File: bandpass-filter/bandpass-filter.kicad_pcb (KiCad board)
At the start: 2 copper layers, 56 x 19 mm, 12 parts, among them J1 Amphenol 10118194-0001LF, J2 Conn_Coaxial, J3 Conn_Coaxial, U1 SKY65015-70LF

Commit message: remove todos
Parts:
- added H1: MountingHole, MountingHole:MountingHole_4.3mm_M4, F.Cu at (98.2, 40.6)
- added H2: MountingHole, MountingHole:MountingHole_4.3mm_M4, F.Cu at (145.2, 40.6)
- added H3: MountingHole, MountingHole:MountingHole_4.3mm_M4, F.Cu at (98.2, 64.6)
- added H4: MountingHole, MountingHole:MountingHole_4.3mm_M4, F.Cu at (145.2, 64.6)
- J1: footprint Connector_USB:USB_Micro-B_Amphenol_10103594-0001LF_Horizontal -> Connector_USB:USB_Micro-B_Amphenol_10118194_Horizontal
- J2, J3: footprint Connector_Coaxial:SMA_Samtec_SMA-J-P-X-ST-EM1_EdgeMount -> Connector_Coaxial:SMA_Molex_73251-2120_EdgeMount_Horizontal
- moved J1 6.64 mm to (107.8, 38.8)
- moved C2 3.73 mm to (105.0, 54.0)
- moved F1 2.86 mm to (138.0, 50.3)
- moved U1 1.22 mm to (110.5, 53.8), turned to 90 degrees
- moved R1 0.39 mm to (116.5, 47.8)
- moved L2 0.30 mm to (116.3, 49.8)
- moved C3 0.28 mm to (116.3, 51.7)
- moved J2 0.06 mm to (95.8, 54.0), turned to 180 degrees
- turned J3 to 0 degrees
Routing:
- net GNDA: track 7.42 -> 0.01 mm, vias 20 -> 23
- net GNDD: track 8.02 -> 1.30 mm
- net Net-(C2-Pad2): track 12.2 -> 8.28 mm
- net +5VD: track 6.88 -> 9.65 mm
- net Net-(C3-Pad2): track 5.83 -> 8.23 mm
- net Net-(F1-Pad5): track 8.73 -> 7.97 mm
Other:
- board size 56 x 19 mm -> 56.1 x 33.2 mm
- net class Default removed

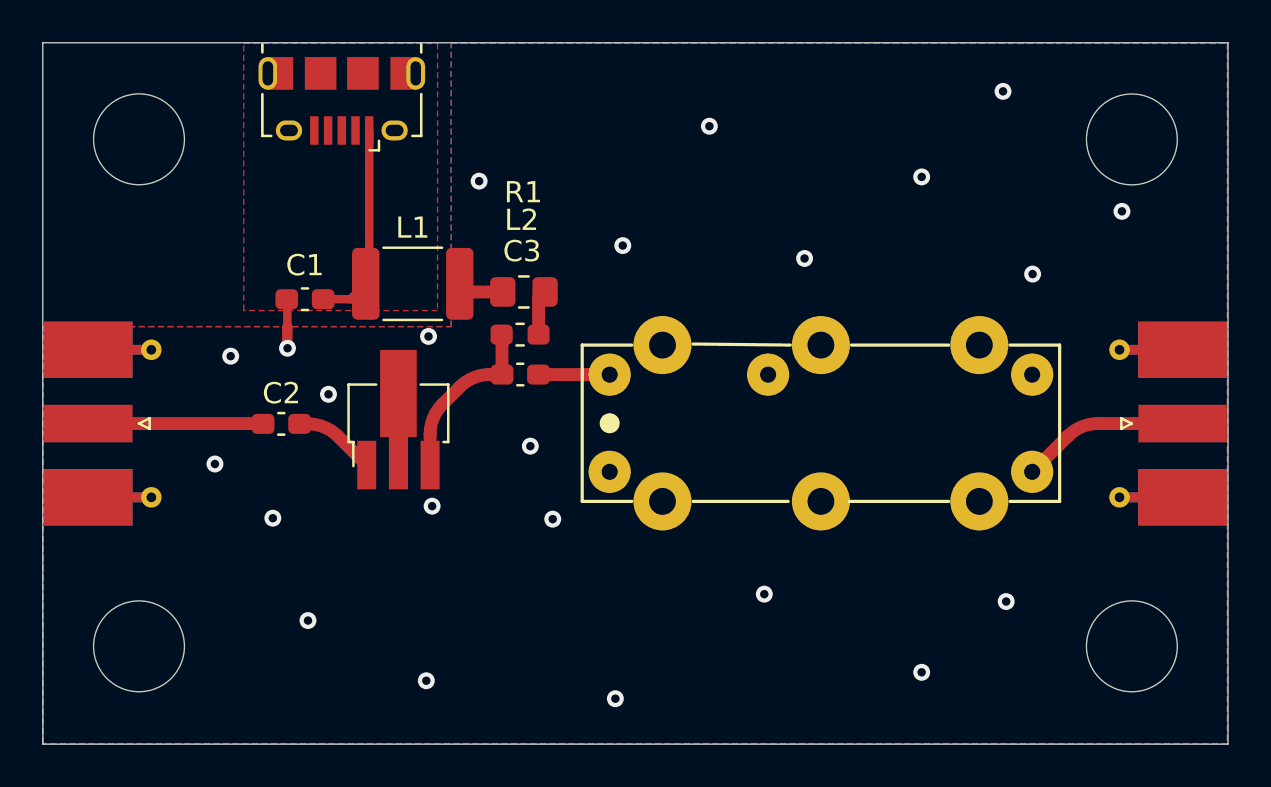
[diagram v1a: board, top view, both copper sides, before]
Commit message: Update PCB with controlled impedance JLCPCB process. Change filter and amplifier order
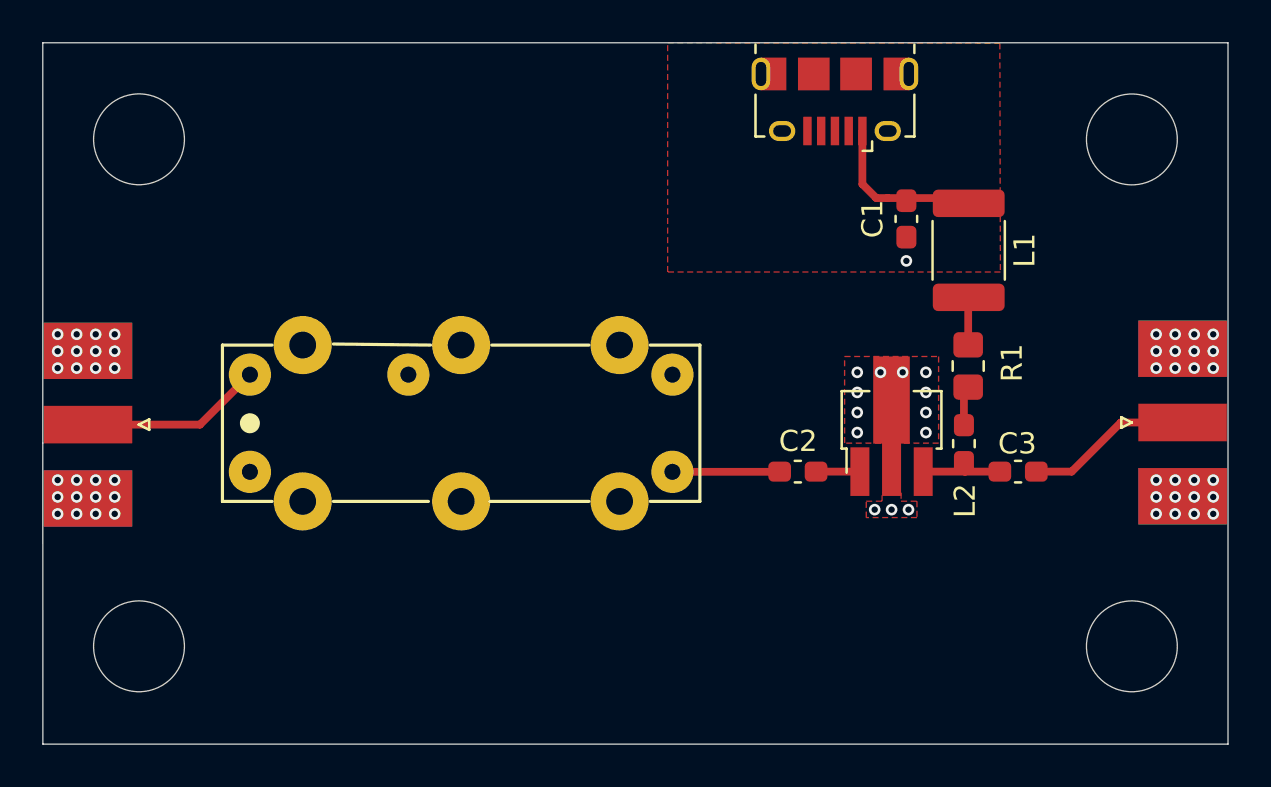
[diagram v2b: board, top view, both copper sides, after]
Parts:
- removed NT1: Net-Tie_2, NetTie:NetTie-2_SMD_Pad0.5mm
- J2, J3: footprint Connector_Coaxial:SMA_Molex_73251-2120_EdgeMount_Horizontal -> sma_connector:sma_connector
- moved C1 28.7 mm to (134.6, 44.3), turned to -90 degrees
- moved L1 26.4 mm to (137.5, 45.8), turned to -90 degrees
- moved C2 24.6 mm to (129.4, 56.3)
- moved C3 24.0 mm to (139.9, 56.3)
- moved U1 23.3 mm to (133.9, 54.1)
- moved J1 23.3 mm to (131.2, 38.8)
- moved L2 21.6 mm to (137.3, 55.0), turned to -90 degrees
- moved R1 21.3 mm to (137.5, 51.3), turned to -90 degrees
- moved F1 17.0 mm to (121.0, 50.3)
- moved J2 2.04 mm to (93.8, 54.0)
- moved J3 2.03 mm to (149.7, 54.0)
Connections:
- C1 pad 2: GNDD -> GNDA
- F1 pad 2: Net-(C3-Pad1) -> Net-(F1-Pad2)
- F1 pad 5: Net-(F1-Pad5) -> Net-(C2-Pad2)
- J1 pad 2: (no net) -> unconnected-(J1-Pad2)
- J1 pad 3: (no net) -> unconnected-(J1-Pad3)
- J1 pad 4: (no net) -> unconnected-(J1-Pad4)
- J1 pad 5: GNDD -> GNDA
- J1 pad 6: GNDD -> GNDA
- J2 pad 1: Net-(C2-Pad2) -> Net-(F1-Pad2)
- J3 pad 1: Net-(F1-Pad5) -> Net-(C3-Pad1)
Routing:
- net Net-(F1-Pad2): track 0.00 -> 8.64 mm
- net Net-(F1-Pad5): track 7.97 -> 0.00 mm
- net Net-(C3-Pad1): track 3.37 -> 7.89 mm
- net Net-(C3-Pad2): track 8.23 -> 4.10 mm
- net Net-(C2-Pad2): track 8.28 -> 5.08 mm
- net +5VD: track 9.65 -> 7.14 mm
- net Net-(C2-Pad1): track 3.89 -> 2.07 mm
- net GNDD: track 1.30 -> 0.00 mm
- net GNDA: track 0.01 -> 0.00 mm, vias 23 -> 62
- added copper zone on In1.Cu, net GNDA
- removed copper zone on B.Cu, net GNDA
- removed copper zone on F.Cu, net GNDD
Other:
- copper layers 2 -> 4
